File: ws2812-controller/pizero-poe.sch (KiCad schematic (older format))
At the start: 61 parts, among them IC1 ENC28J60-I/ML, J1 RJ45-LED, P1 Raspberry_Pi_+_Conn, P2 WS2812 Cn., P3 WS2812 Cn., Q1 SI3440DV, Q3 BSS138, T1 PULSE_H1197, T2 TRANSFO, T3 VOLTAGE_REF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

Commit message: added half of component part numbers
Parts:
- C1, C10, C7, C8, C9: Mouser Part No. (none) -> 710-885012105001
- C11: value C -> 10uf; footprint w_smd_cap:c_0402 -> w_smd_cap:c_0603; Mouser Part No. (none) -> 81-ZRB18AR61C106ME1L
- C17: Mouser Part No. (none) -> 667-EEE-1AA221P
- C19: Mouser Part No. 810-C1005X5R1H104K -> 710-885012105001
- C2, C3: value C -> 16pf; Mouser Part No. (none) -> 81-GRM1555C1H160JA1D
- D7: Mouser Part No. (none) -> 771-BZT52HB5V1115
- IC1: Mouser Part No. (none) -> 579-ENC28J60-I/ML
- J1: Mouser Part No. (none) -> 710-615008137421
- Q3: Mouser Part No. (none) -> 512-BSS138
- R23, R24: Mouser Part No. (none) -> 667-ERJ-2RKF1402X
- R25: value R -> 100; Mouser Part No. (none) -> 71-CRCW0402-100-E3
- R3: value R -> 1k; Mouser Part No. (none) -> 754-RR0510P-102D
- R8: value R -> 2.32k; Mouser Part No. (none) -> 667-ERJ-2RKF2321X
- Y1: Mouser Part No. 732-322525MF10P-C -> 774-445I23D25M00000
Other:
- note added: "BOM DONE"
- note removed: "3.3v @ 1.5A LDO supply"

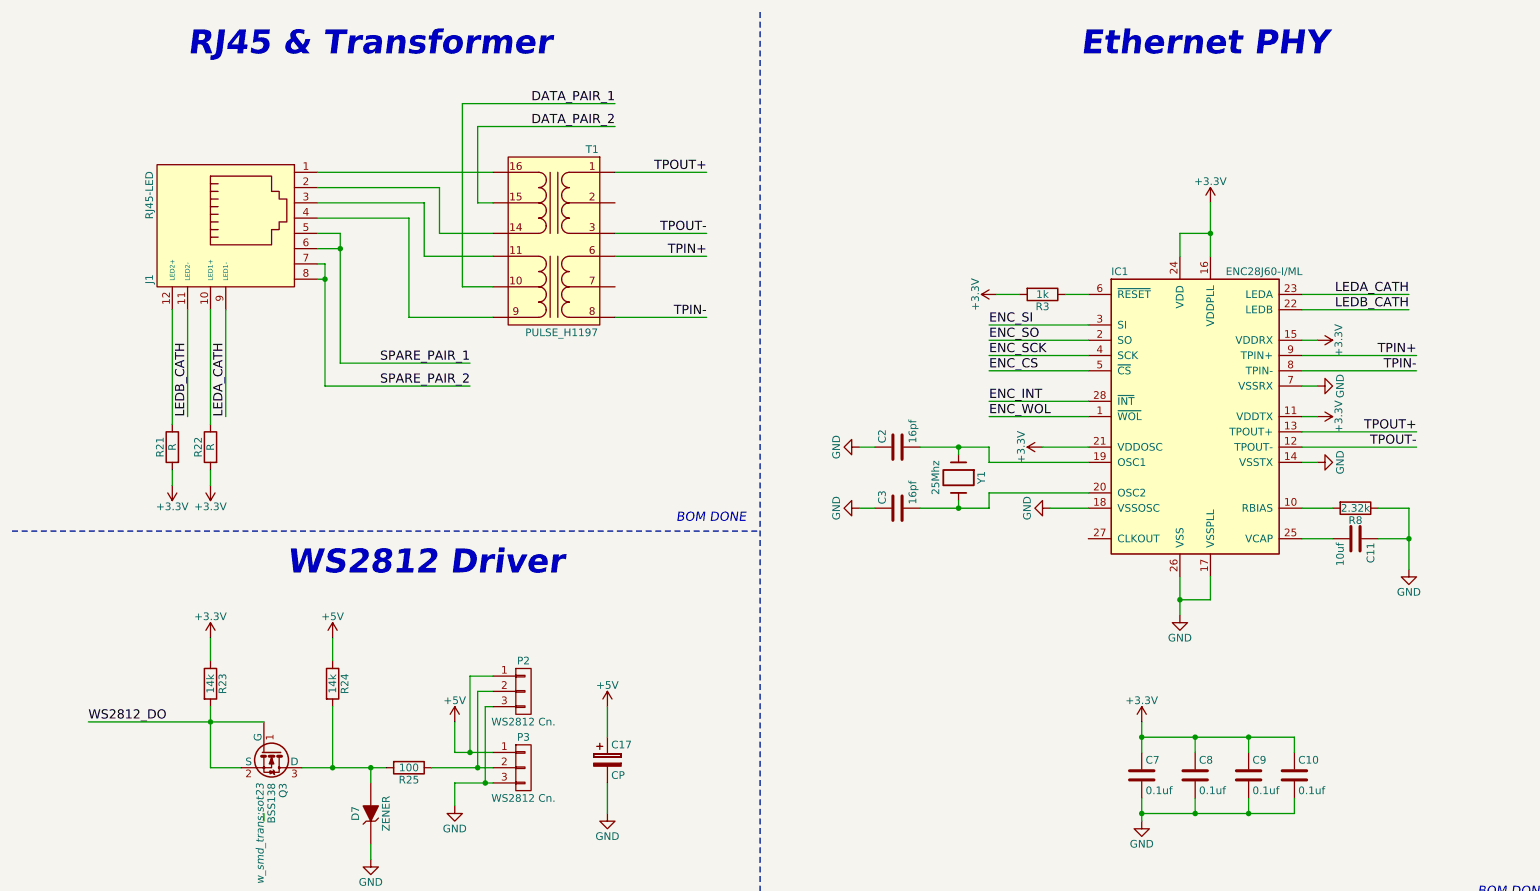
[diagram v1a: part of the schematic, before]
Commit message: added EMI filtering on data lines
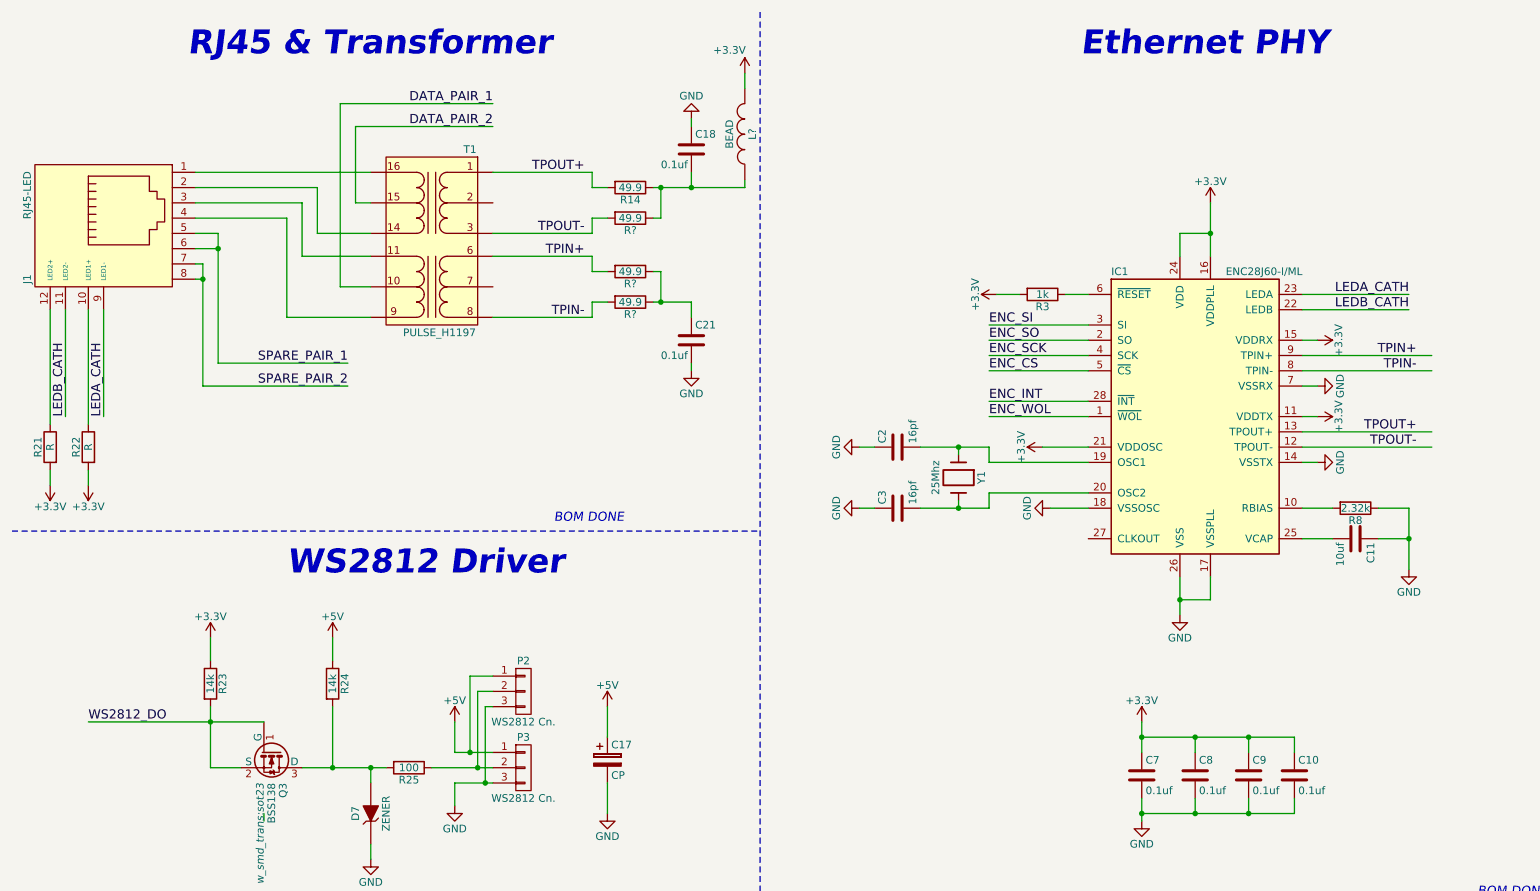
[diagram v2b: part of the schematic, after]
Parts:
- added C18, C21: 0.1uf, w_smd_cap:c_0603, symbol C
- added L?: BEAD, w_smd_inductors:inductor_smd_0402, symbol INDUCTOR
- added R14, R? (x3): 49.9, w_smd_resistors:r_0402, symbol R
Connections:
- net +3V3: now also L?.2
- net GND: now also C18.1, C21.2
- net TPIN+: now also R?.2
- net TPIN-: now also R?.2
- net TPOUT+: now also R14.2
- net TPOUT-: now also R?.2
- new net: C18.2, L?.1, R14.1, R?.1
- new net: C21.1, R?.1, R?.1
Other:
- moved on the sheet: J1, R21, R22, T1

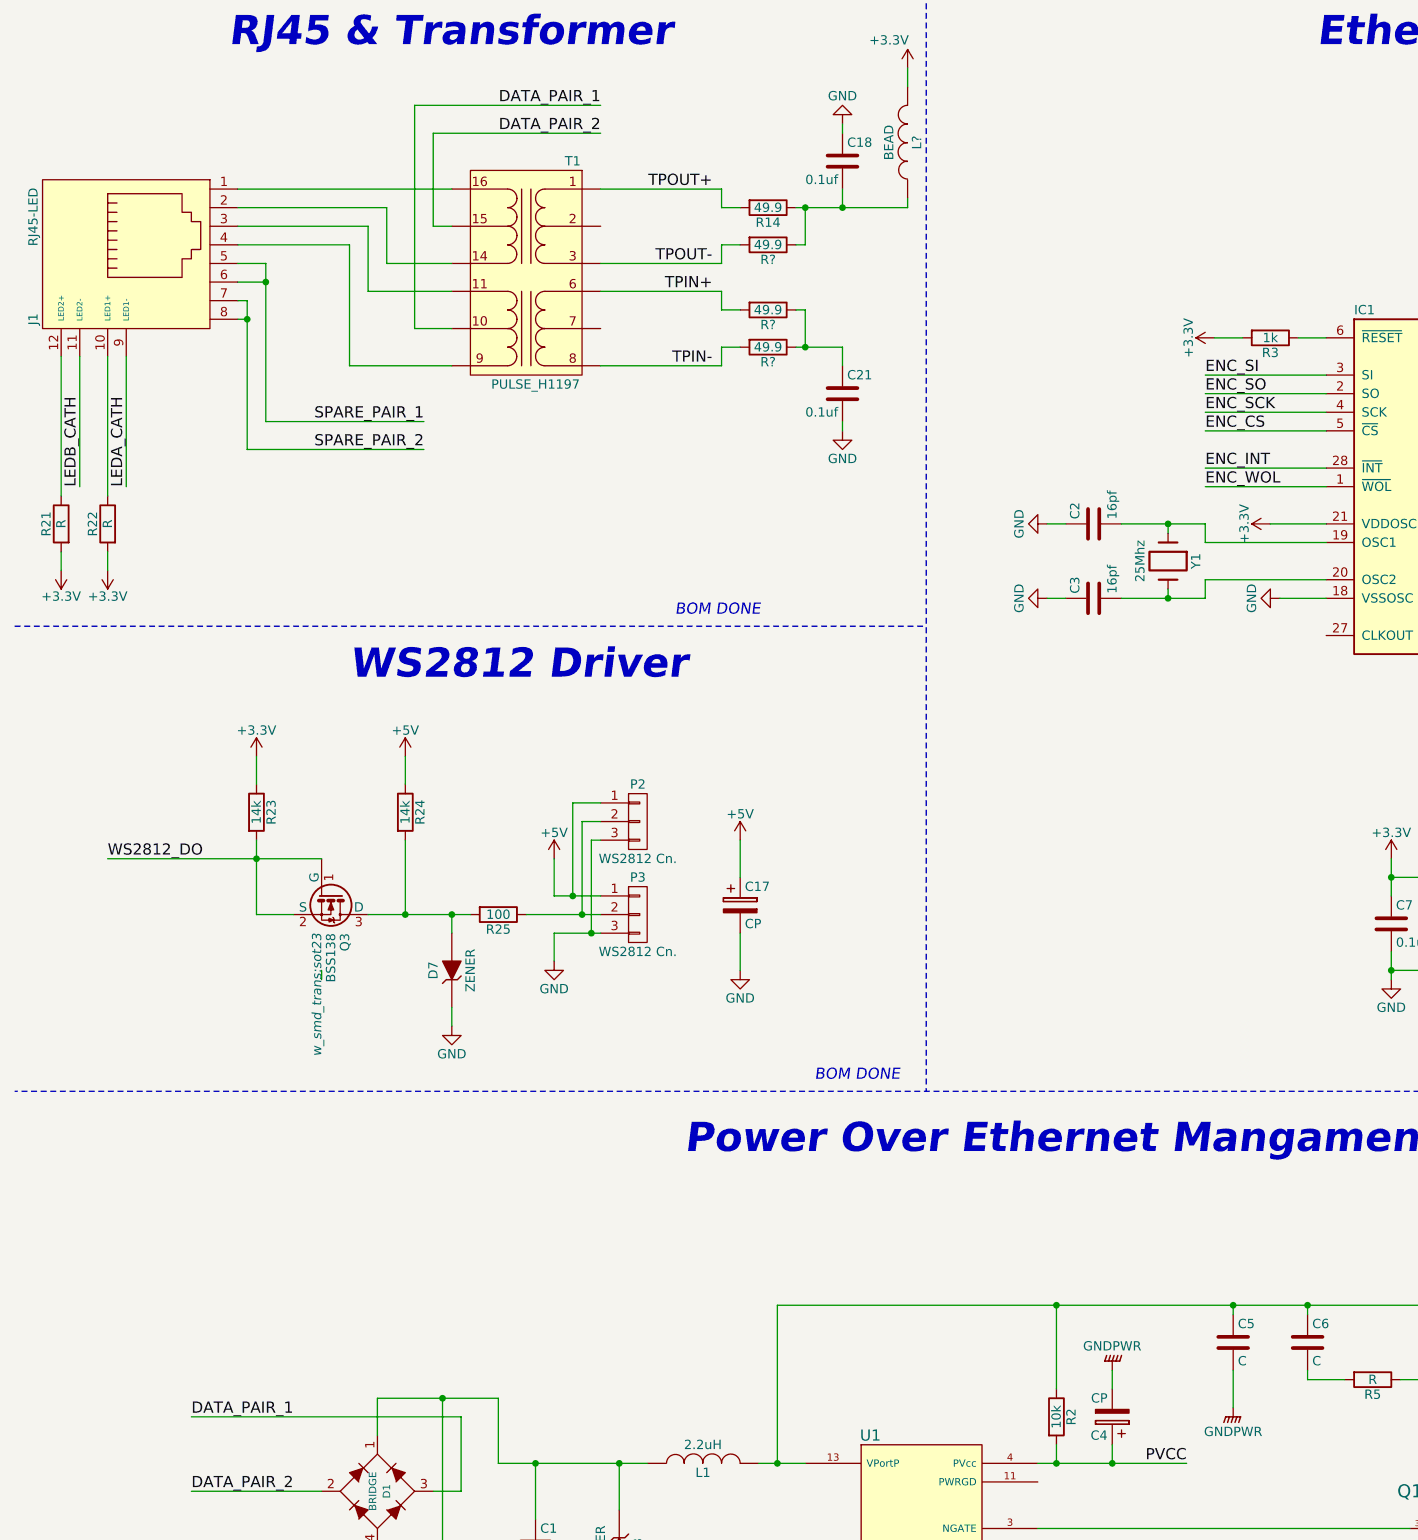
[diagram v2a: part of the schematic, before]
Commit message: changed caps after reviewing notes
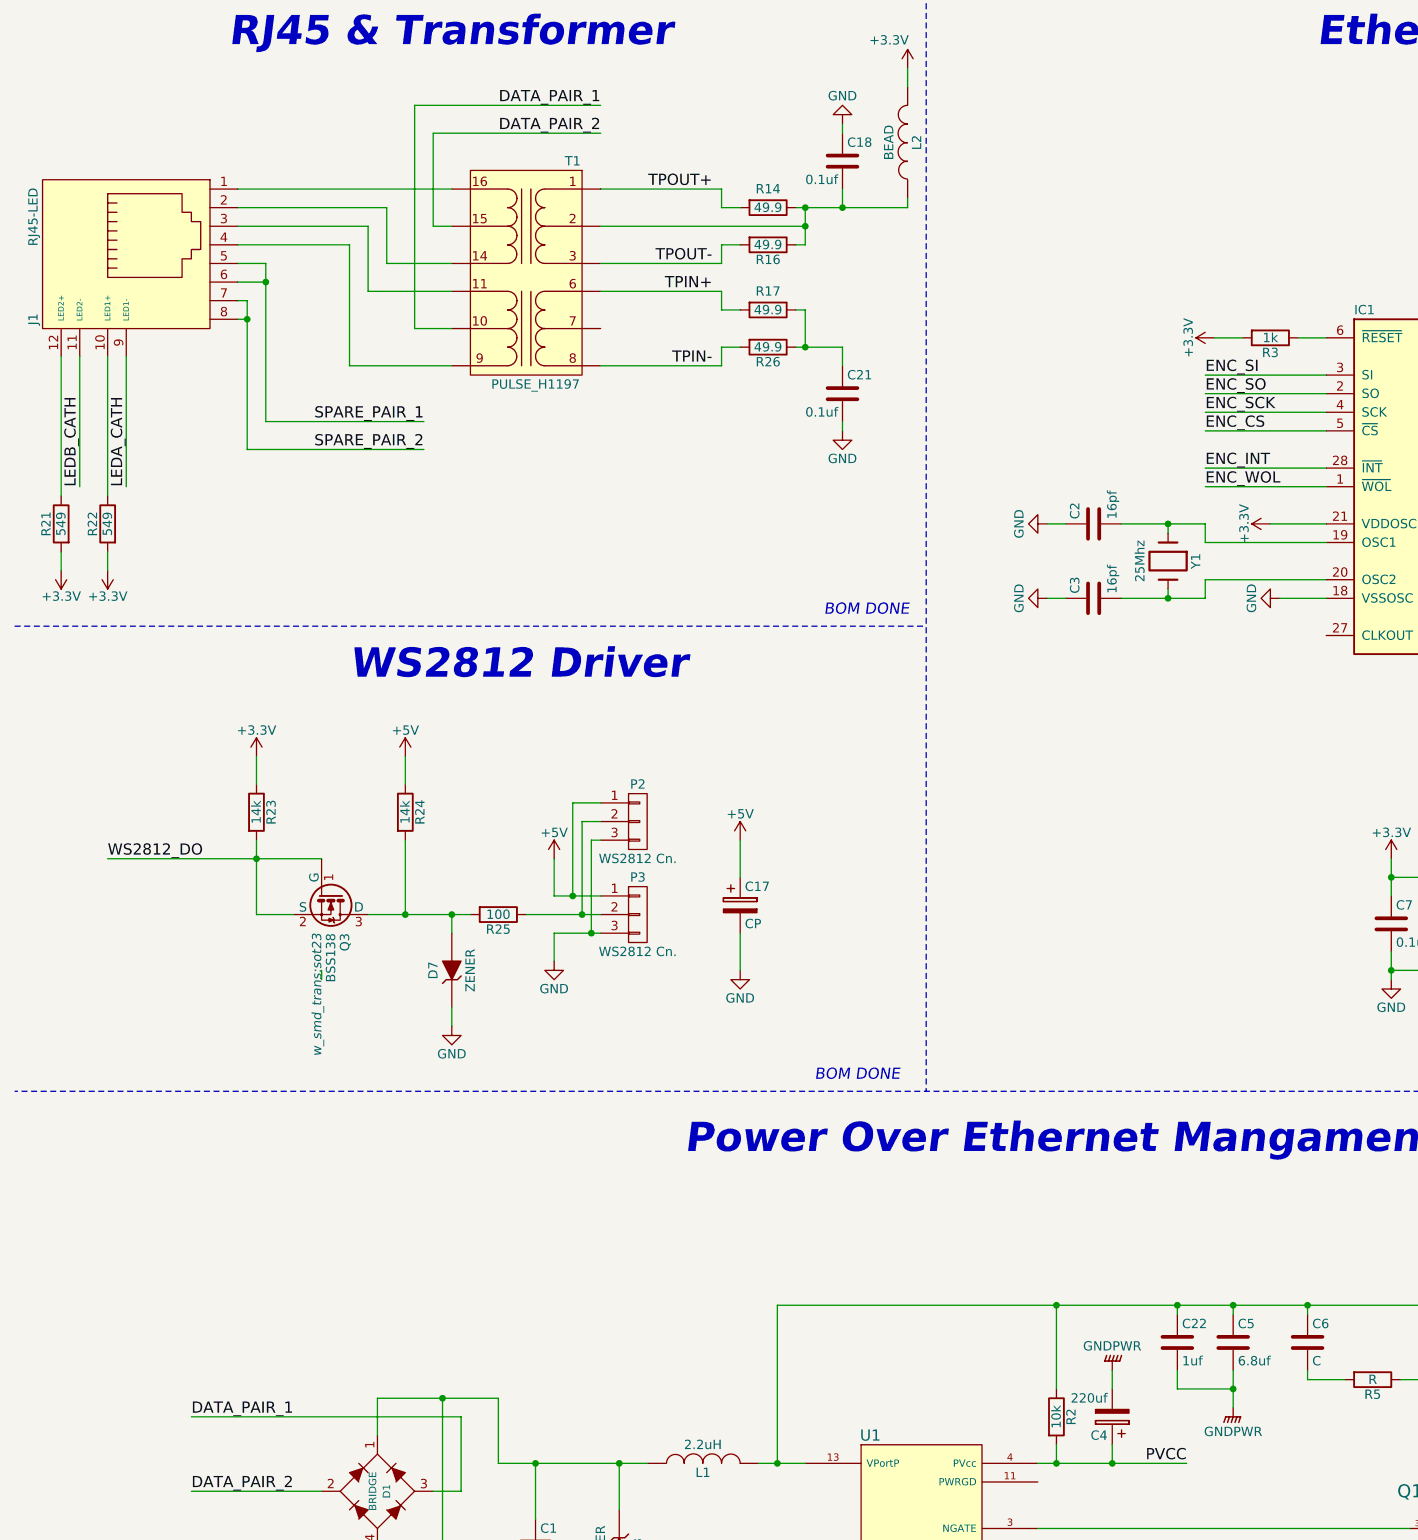
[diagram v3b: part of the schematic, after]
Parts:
- added C22: 1uf, w_smd_cap:c_0805, symbol C
- C18, C21: footprint w_smd_cap:c_0603 -> w_smd_cap:c_0402
- C4: value CP -> 220uf; Mouser Part No. (none) -> 581-TAJB475K025R
- C5: value C -> 6.8uf; footprint w_smd_cap:c_0402 -> w_smd_cap:c_tant_D; Mouser Part No. (none) -> 74-293D685X9050D2TE3
- R21, R22: value R -> 549; Mouser Part No. (none) -> 667-ERJ-2RKF5490X
- U1: Digikey Part No. (none) -> LTC4267CGN-3#PBF-ND
- gave numbers to parts that had none: 4
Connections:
- net GNDPWR: now also C22.2
- net at C5.1, C6.1, L1.2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: now also C22.1
- net at T1.2 (PM): now also C18.2, L2.1, R14.1, R16.1

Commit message: first complete development revision
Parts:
- C12: Mouser Part No. (none) -> 667-EEE-1AA330WR
- C13: Mouser Part No. (none) -> 81-GRM1885C1H202JA1D
- C14: value C -> 6.8nf; Mouser Part No. (none) -> 81-GRM155R71H682KA8D
- C15, C16: value C -> 0.1uf; footprint w_smd_cap:c_0402 -> w_smd_cap:c_0603; Mouser Part No. (none) -> 710-885012105001
- R1: value 68.1 -> DNP
- R10, R11, R4: value R -> 10k; Mouser Part No. (none) -> 754-RR0510P-103D
- R12: value R -> 3.3k; Mouser Part No. (none) -> 754-RR0510P-332D
- R2: Mouser Part No. (none) -> 754-RR0510P-103D
- R6: Mouser Part No. (none) -> 660-UR732BTTD50L0F
- R7: value R -> 6.8k; Mouser Part No. (none) -> 754-RR0510P-682D
- R9: value R -> 1k
- T3: Mouser Part No. (none) -> 863-TLV431BSN1T1G
